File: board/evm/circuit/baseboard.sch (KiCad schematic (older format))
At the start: 20 parts

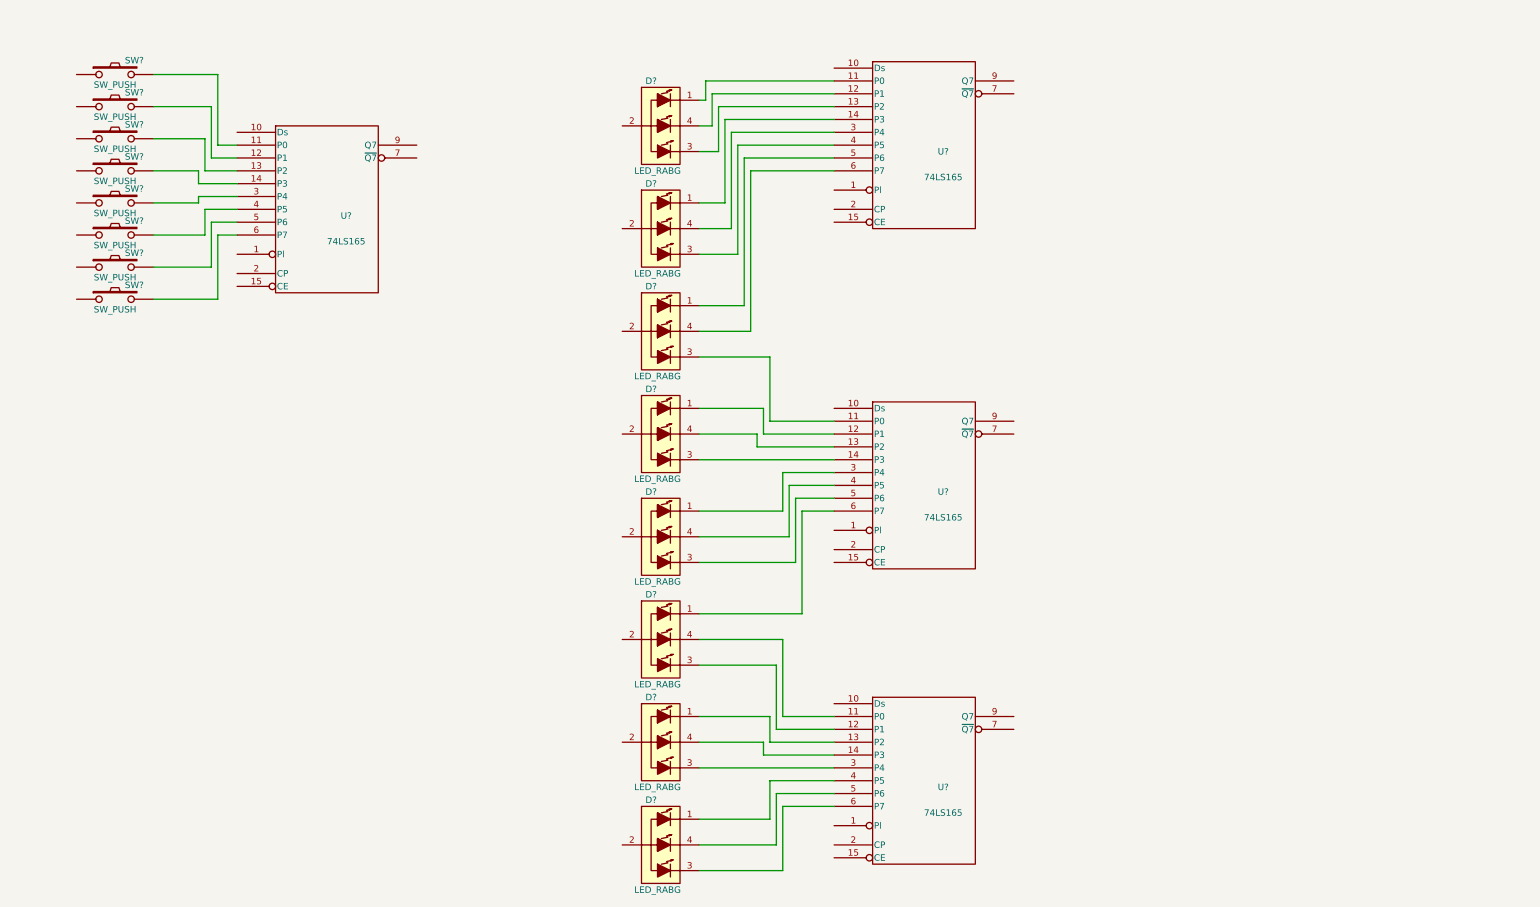
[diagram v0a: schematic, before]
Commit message: add cpld
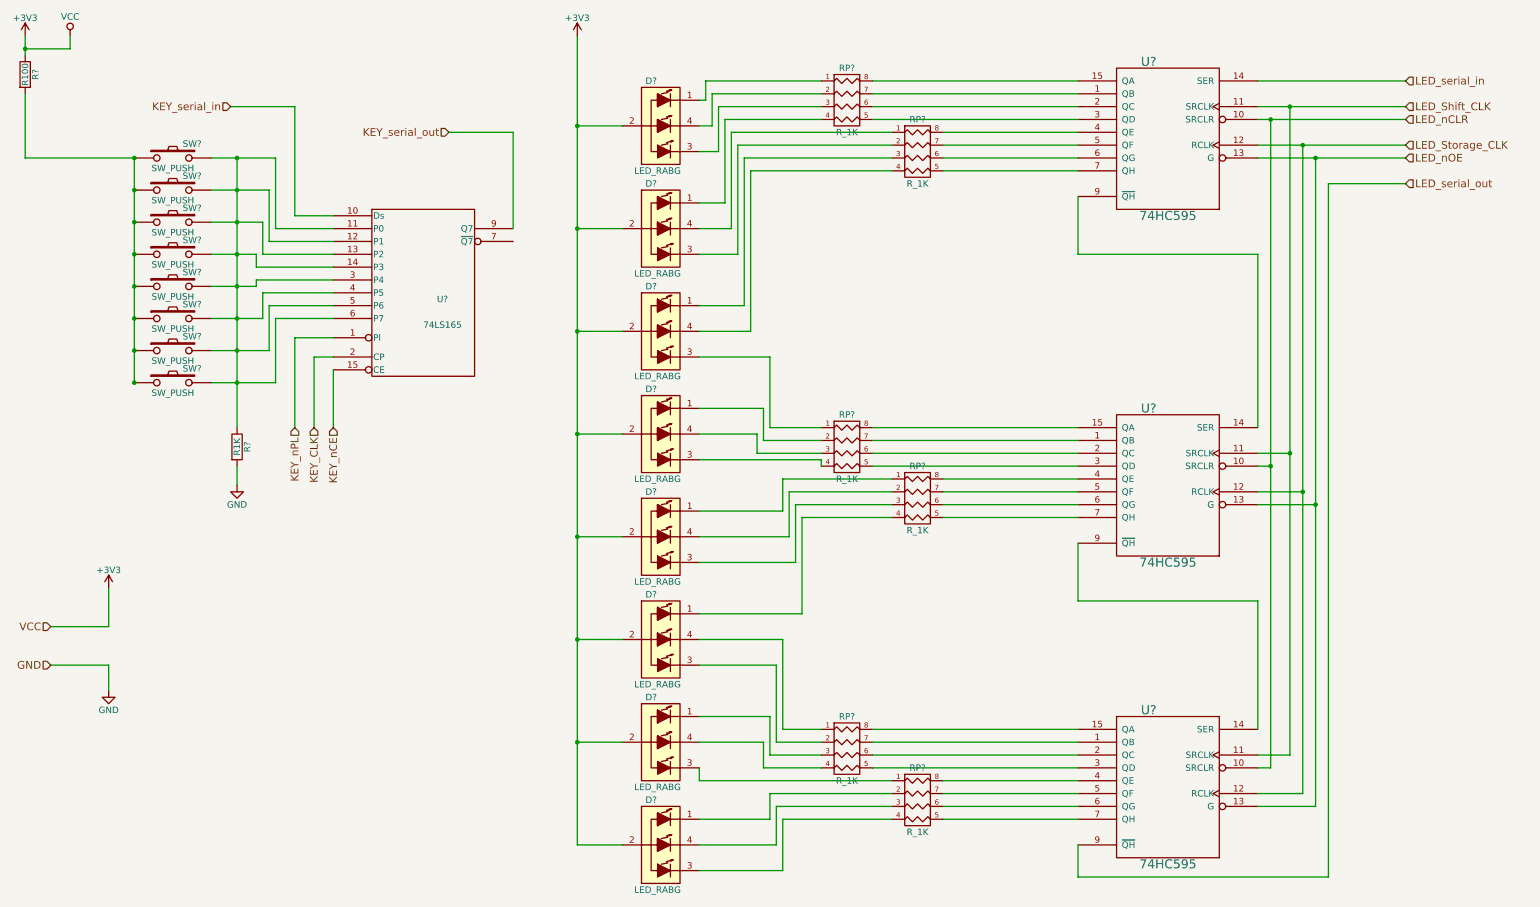
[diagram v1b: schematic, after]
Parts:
- removed U? (x3): 74LS165, symbol 74LS165
- added R?: R100, symbol R
- added R?: R1K, symbol R
- added RP? (x6): R_1K, symbol R_PACK4
- added U? (x3): 74HC595, symbol 74HC595
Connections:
- net VCC is gone; now on net +3V3: U?.16 (VCC)
- net GND: now also R?.2, U?.8 (GND), U?.8 (GND), U?.8 (GND)
- net KEY_nPL: now reaches U?.1 (Pl)
- net KEY_serial_in: now reaches U?.10 (Ds)
- net at SW?.2, U?.11 (P0): now also SW?.2, SW?.2, SW?.2, SW?.2, SW?.2, SW?.2, SW?.2, U?.12 (P1), U?.13 (P2), U?.14 (P3), U?.3 (P4), U?.4 (P5), U?.5 (P6), U?.6 (P7), R?.1
- net KEY_nCE: now reaches U?.15 (CE)
- net KEY_CLK: now reaches U?.2 (CP)
- net KEY_serial_out: now reaches U?.9 (Q7)
- net at SW?.1: now also SW?.1, SW?.1, SW?.1, SW?.1, SW?.1, SW?.1, SW?.1, R?.2
- net at D?.1 (RED_CATHODE): now also RP?.1 (P1) (x2)
- net +3V3: now reaches D?.2 (COMMON_ANODE)
- net +3V3: now also D?.2 (COMMON_ANODE), D?.2 (COMMON_ANODE), D?.2 (COMMON_ANODE), D?.2 (COMMON_ANODE), D?.2 (COMMON_ANODE), D?.2 (COMMON_ANODE), D?.2 (COMMON_ANODE), R?.1, U?.16 (VCC), U?.16 (VCC), U?.16 (VCC)
- net at D?.3 (BLUE_CATHODE): now also RP?.3 (P3) (x2)
- net at D?.4 (GREEN_CATHODE): now also RP?.2 (P2) (x2)
- net at D?.1 (RED_CATHODE): now also RP?.4 (P4) (x2)
- net at D?.3 (BLUE_CATHODE): now also RP?.2 (P2) (x2)
- net at D?.4 (GREEN_CATHODE): now also RP?.1 (P1) (x2)
- net at D?.1 (RED_CATHODE): now also RP?.3 (P3) (x2)
- net at D?.3 (BLUE_CATHODE): now also RP?.1 (P1) (x2)
- net at D?.4 (GREEN_CATHODE): now also RP?.4 (P4) (x2)
- net at D?.1 (RED_CATHODE): now also RP?.2 (P2) (x2)
- net at D?.3 (BLUE_CATHODE): now also RP?.4 (P4) (x2)
- net at D?.4 (GREEN_CATHODE): now also RP?.3 (P3) (x2)
- new net: RP?.5 (R4), U?.3 (QD) (x3)
- new net: RP?.6 (R3), U?.2 (QC) (x3)
- new net: RP?.7 (R2), U?.1 (QB) (x3)
- new net: RP?.8 (R1), U?.15 (QA) (x3)
- new net: RP?.5 (R4), U?.7 (QH) (x3)
- new net: RP?.6 (R3), U?.6 (QG) (x3)
- new net: RP?.7 (R2), U?.5 (QF) (x3)
- new net: RP?.8 (R1), U?.4 (QE) (x3)
- new net: U?.14 (SER), U?.9 (~QH) (x2)
- new net LED_Shift_CLK: U?.11 (SRCLK), U?.11 (SRCLK), U?.11 (SRCLK)
- new net LED_Storage_CLK: U?.12 (RCLK), U?.12 (RCLK), U?.12 (RCLK)
- new net LED_nCLR: U?.10 (SRCLR), U?.10 (SRCLR), U?.10 (SRCLR)
- new net LED_nOE: U?.13 (G), U?.13 (G), U?.13 (G)
- new net LED_serial_in: U?.14 (SER)
- new net LED_serial_out: U?.9 (~QH)
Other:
- moved on the sheet: SW?, U?

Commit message: basic works for mcu
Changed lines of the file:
@@
 LIBS:contrib
 LIBS:valves
-LIBS:stm8
-LIBS:stm32
-LIBS:74xgxx
-LIBS:ac-dc
-LIBS:actel
 LIBS:Altera
-LIBS:analog_devices
-LIBS:battery_management
-LIBS:bbd
-LIBS:brooktre
-LIBS:cmos_ieee
-LIBS:dc-dc
-LIBS:diode
-LIBS:elec-unifil
-LIBS:ESD_Protection
-LIBS:ftdi
-LIBS:gennum
-LIBS:graphic
-LIBS:hc11
-LIBS:ir
-LIBS:Lattice
-LIBS:logo
-LIBS:maxim
-LIBS:microchip_dspic33dsc
-LIBS:microchip_pic10mcu
-LIBS:microchip_pic12mcu
-LIBS:microchip_pic16mcu
-LIBS:microchip_pic18mcu
-LIBS:microchip_pic32mcu
-LIBS:motor_drivers
-LIBS:msp430
-LIBS:nordicsemi
-LIBS:nxp_armmcu
-LIBS:onsemi
-LIBS:Oscillators
-LIBS:powerint
-LIBS:Power_Management
-LIBS:pspice
-LIBS:references
-LIBS:relays
-LIBS:rfcom
-LIBS:sensors
-LIBS:silabs
-LIBS:supertex
-LIBS:switches
-LIBS:transf
-LIBS:ttl_ieee
-LIBS:video
-LIBS:Worldsemi
-LIBS:Xicor
-LIBS:Zilog
 LIBS:my_kicad
 LIBS:oh-my-keyboard-cache
@@
 LED_serial_out
 Wire Wire Line
-	2200 1850 2400 1850
-Wire Wire Line
-	2400 1850 2700 1850
+	2200 1850 2700 1850
 Wire Wire Line
 	2700 1850 2700 2400
@@
 	2700 2400 3150 2400
 Wire Wire Line
-	2200 2100 2400 2100
-Wire Wire Line
-	2400 2100 2650 2100
+	2200 2100 2650 2100
 Wire Wire Line
 	2650 2100 2650 2500
@@
 	2650 2500 3150 2500
 Wire Wire Line
-	2200 2350 2400 2350
-Wire Wire Line
-	2400 2350 2600 2350
+	2200 2350 2600 2350
 Wire Wire Line
 	2600 2350 2600 2600
@@
 	3150 2700 2550 2700
 Wire Wire Line
-	2550 2700 2550 2600
-Wire Wire Line
-	2550 2600 2400 2600
-Wire Wire Line
-	2400 2600 2200 2600
-Wire Wire Line
-	2200 2850 2400 2850
-Wire Wire Line
-	2400 2850 2550 2850
+	2550 2600 2550 2700
+Wire Wire Line
+	2200 2600 2550 2600
+Wire Wire Line
+	2200 2850 2550 2850
 Wire Wire Line
 	2550 2850 2550 2800
@@
 	3150 2900 2600 2900
 Wire Wire Line
-	2600 2900 2600 3100
-Wire Wire Line
-	2600 3100 2400 3100
-Wire Wire Line
-	2400 3100 2200 3100
+	2600 3100 2600 2900
+Wire Wire Line
+	2200 3100 2600 3100
 Wire Wire Line
 	3150 3000 2650 3000
 Wire Wire Line
-	2650 3000 2650 3350
-Wire Wire Line
-	2650 3350 2400 3350
-Wire Wire Line
-	2400 3350 2200 3350
-Wire Wire Line
-	2200 3600 2400 3600
-Wire Wire Line
-	2400 3600 2700 3600
+	2650 3350 2650 3000
+Wire Wire Line
+	2200 3350 2650 3350
+Wire Wire Line
+	2200 3600 2700 3600
 Wire Wire Line
 	2700 3600 2700 3100
@@
 	1400 5500 1400 5200
 Wire Wire Line
-	750  1050 750  1000
-Wire Wire Line
-	750  1000 750  900
+	750  900  750  1050
 Wire Wire Line
 	750  1350 750  1850
@@
 	750  1850 1600 1850
 Wire Wire Line
-	1600 1850 1600 2100
-Wire Wire Line
-	1600 2100 1600 2350
-Wire Wire Line
-	1600 2350 1600 2600
-Wire Wire Line
-	1600 2600 1600 2850
-Wire Wire Line
-	1600 2850 1600 3100
-Wire Wire Line
-	1600 3100 1600 3350
-Wire Wire Line
-	1600 3350 1600 3600
+	1600 1850 1600 3600
 Connection ~ 1600 1850
 Wire Wire Line
 	2400 4400 2400 4250
 Wire Wire Line
-	2400 1850 2400 2100
-Wire Wire Line
-	2400 2100 2400 2350
-Wire Wire Line
-	2400 2350 2400 2600
-Wire Wire Line
-	2400 2600 2400 2850
-Wire Wire Line
-	2400 2850 2400 3100
-Wire Wire Line
-	2400 3100 2400 3350
-Wire Wire Line
-	2400 3350 2400 3600
-Wire Wire Line
-	2400 3600 2400 3950
+	2400 1850 2400 3950
 Connection ~ 1600 3600
 Connection ~ 2400 1850
@@
 Connection ~ 2400 3350
 Wire Wire Line
-	5050 900  5050 1600
-Wire Wire Line
-	5050 1600 5050 2400
-Wire Wire Line
-	5050 2400 5050 3200
-Wire Wire Line
-	5050 3200 5050 4000
-Wire Wire Line
-	5050 4000 5050 4800
-Wire Wire Line
-	5050 4800 5050 5600
-Wire Wire Line
-	5050 5600 5050 6400
-Wire Wire Line
-	5050 6400 5050 7200
+	5050 900  5050 7200
 Wire Wire Line
 	5050 7200 5400 7200
@@
 	10600 6500 10350 6500
 Wire Wire Line
-	10600 1450 10600 4150
-Wire Wire Line
-	10600 4150 10600 6500
+	10600 1450 10600 6500
 Wire Wire Line
 	10600 4150 10350 4150
 Wire Wire Line
-	10350 1450 10600 1450
-Wire Wire Line
-	10600 1450 11500 1450
+	10350 1450 11500 1450
 Connection ~ 10600 4150
 Connection ~ 10600 1450
@@
 	11500 1250 10350 1250
 Wire Wire Line
-	11500 1550 10450 1550
-Wire Wire Line
-	10450 1550 10350 1550
-Wire Wire Line
-	11500 1750 10700 1750
-Wire Wire Line
-	10700 1750 10350 1750
-Wire Wire Line
-	10350 1850 10800 1850
-Wire Wire Line
-	10800 1850 11500 1850
+	10350 1550 11500 1550
+Wire Wire Line
+	10350 1750 11500 1750
+Wire Wire Line
+	10350 1850 11500 1850
 Wire Wire Line
 	10350 4250 10450 4250
 Wire Wire Line
-	10450 1550 10450 4250
-Wire Wire Line
-	10450 4250 10450 6600
+	10450 1550 10450 6600
 Connection ~ 10450 1550
 Wire Wire Line
 	10350 4450 10700 4450
 Wire Wire Line
-	10700 1750 10700 4450
-Wire Wire Line
-	10700 4450 10700 6800
+	10700 1750 10700 6800
 Connection ~ 10700 1750
 Wire Wire Line
 	10350 4550 10800 4550
 Wire Wire Line
-	10800 1850 10800 4550
-Wire Wire Line
-	10800 4550 10800 6900
+	10800 1850 10800 6900
 Connection ~ 10800 1850
 Wire Wire Line
